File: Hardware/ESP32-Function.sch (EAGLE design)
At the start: 36 parts, among them J1 MICROMOD_STANDARD, Q2 MBT3904DW1T1, U1 EEPROM, U2 ESP-WROOM-3232D-NARROW, U3 3.3V, U4 CP210X

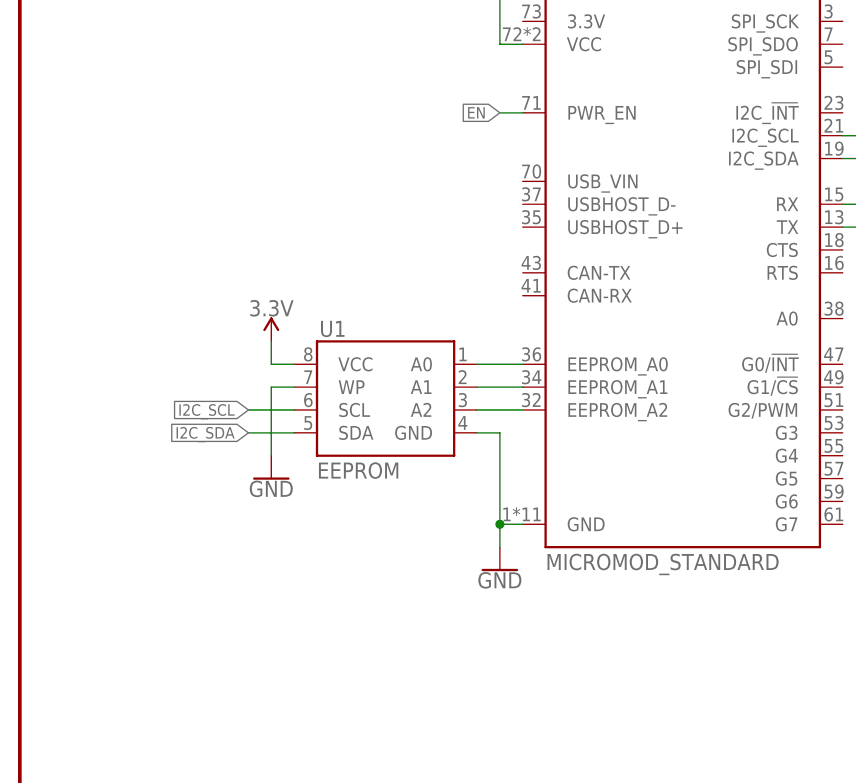
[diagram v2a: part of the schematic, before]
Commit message: Adds pullup resistor and jumper to write protect net, brings write protect trace to card's edge
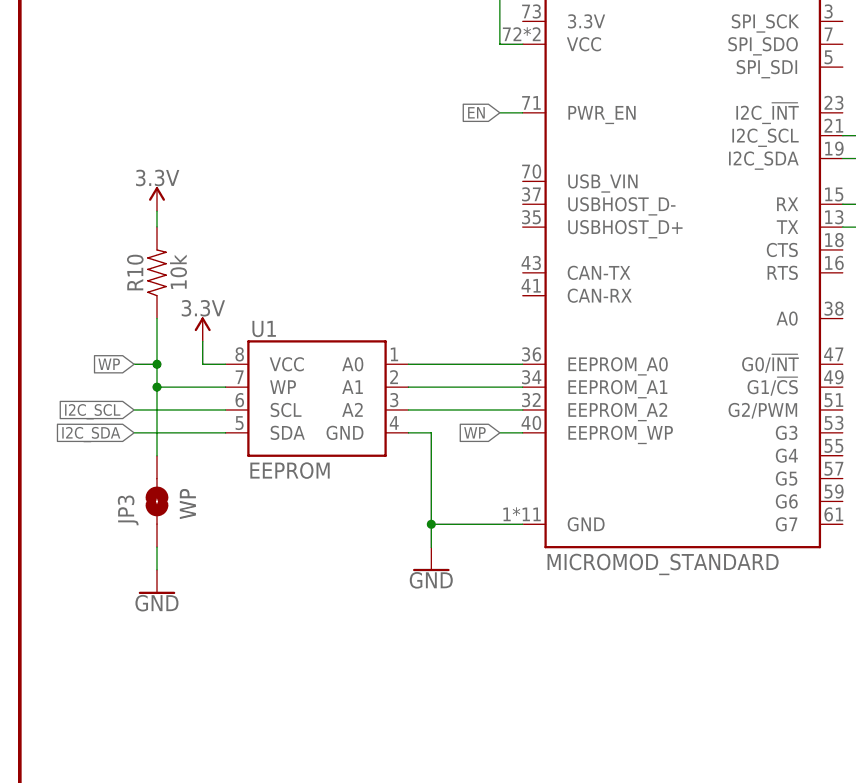
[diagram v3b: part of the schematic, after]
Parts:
- added JP3: JUMPER-SMT_2_NO_SILK, SparkFun-Jumpers:JUMPER-SMT_2_NO_SILK
- added R10: 10k, SparkFun-Resistors:10KOHM-0603-1/10W-1%
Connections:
- new net WP: J1.EEPROM_WP, JP3.2, R10.1, U1.WP
- net 3.3V: now also R10.2
- net GND: now also JP3.1; no longer U1.WP
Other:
- note added: "WP"
- moved on the sheet: U1
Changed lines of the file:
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@@
 <part name="R8" library="SparkFun-Resistors" deviceset="4.7KOHM" device="-0603-1/10W-1%" value="4.7k"/>
 <part name="R9" library="SparkFun-Resistors" deviceset="4.7KOHM" device="-0603-1/10W-1%" value="4.7k"/>
+<part name="R10" library="SparkFun-Resistors" deviceset="10KOHM" device="-0603-1/10W-1%" value="10k"/>
+<part name="JP3" library="SparkFun-Jumpers" deviceset="JUMPER-SMT_2_NO" device="_SILK" package3d_urn="urn:adsk.eagle:package:39279/1"/>
+<part name="SUPPLY10" library="SparkFun-PowerSymbols" deviceset="3.3V" device=""/>
 </parts>
 <sheets>
@@
 remove I2C data line and/or
 clock from pullup resistors.</text>
+<text x="19.558" y="64.008" size="1.778" layer="97" font="vector" rot="R90">WP</text>
 </plain>
 <instances>
@@
 <attribute name="VALUE" x="58.42" y="58.42" size="1.778" layer="96" font="vector"/>
 </instance>
-<instance part="GND1" gate="1" x="53.34" y="58.42" smashed="yes">
-<attribute name="VALUE" x="53.34" y="58.166" size="1.778" layer="96" font="vector" align="top-center"/>
+<instance part="GND1" gate="1" x="45.72" y="58.42" smashed="yes">
+<attribute name="VALUE" x="45.72" y="58.166" size="1.778" layer="96" font="vector" align="top-center"/>
 </instance>
 <instance part="R2" gate="G$1" x="185.42" y="124.46" smashed="yes" rot="R90">
@@
 <attribute name="VALUE" x="274.32" y="59.182" size="1.778" layer="96" font="vector" align="bottom-center"/>
 </instance>
-<instance part="U1" gate="G$1" x="40.64" y="76.2" smashed="yes" rot="MR0">
-<attribute name="NAME" x="33.274" y="84.328" size="1.778" layer="95" font="vector"/>
-<attribute name="VALUE" x="33.02" y="68.58" size="1.778" layer="96" font="vector"/>
-</instance>
-<instance part="SUPPLY3" gate="G$1" x="27.94" y="83.82" smashed="yes">
-<attribute name="VALUE" x="27.94" y="86.614" size="1.778" layer="96" font="vector" align="bottom-center"/>
-</instance>
-<instance part="GND15" gate="1" x="27.94" y="68.58" smashed="yes">
-<attribute name="VALUE" x="27.94" y="68.326" size="1.778" layer="96" font="vector" align="top-center"/>
+<instance part="U1" gate="G$1" x="33.02" y="76.2" smashed="yes" rot="MR0">
+<attribute name="NAME" x="25.654" y="84.328" size="1.778" layer="95" font="vector"/>
+<attribute name="VALUE" x="25.4" y="68.58" size="1.778" layer="96" font="vector"/>
+</instance>
+<instance part="SUPPLY3" gate="G$1" x="20.32" y="83.82" smashed="yes">
+<attribute name="VALUE" x="20.32" y="86.614" size="1.778" layer="96" font="vector" align="bottom-center"/>
+</instance>
+<instance part="GND15" gate="1" x="15.24" y="55.88" smashed="yes">
+<attribute name="VALUE" x="15.24" y="55.626" size="1.778" layer="96" font="vector" align="top-center"/>
 </instance>
 <instance part="U2" gate="U1" x="213.36" y="83.82" smashed="yes">
@@
 <attribute name="NAME" x="366.776" y="195.58" size="1.778" layer="95" font="vector" rot="R90" align="bottom-center"/>
 <attribute name="VALUE" x="369.824" y="195.58" size="1.778" layer="96" font="vector" rot="R90" align="top-center"/>
+</instance>
+<instance part="R10" gate="G$1" x="15.24" y="91.44" smashed="yes" rot="R90">
+<attribute name="NAME" x="13.716" y="91.44" size="1.778" layer="95" font="vector" rot="R90" align="bottom-center"/>
+<attribute name="VALUE" x="16.764" y="91.44" size="1.778" layer="96" font="vector" rot="R90" align="top-center"/>
+</instance>
+<instance part="JP3" gate="G$1" x="15.24" y="66.04" smashed="yes" rot="R90">
+<attribute name="NAME" x="12.7" y="63.5" size="1.778" layer="95" font="vector" rot="R90"/>
+</instance>
+<instance part="SUPPLY10" gate="G$1" x="15.24" y="98.298" smashed="yes">
+<attribute name="VALUE" x="15.24" y="101.092" size="1.778" layer="96" font="vector" align="bottom-center"/>
 </instance>
 </instances>
@@
 <segment>
 <pinref part="U1" gate="G$1" pin="VCC"/>
-<wire x1="30.48" y1="81.28" x2="27.94" y2="81.28" width="0.1524" layer="91"/>
+<wire x1="22.86" y1="81.28" x2="20.32" y2="81.28" width="0.1524" layer="91"/>
 <pinref part="SUPPLY3" gate="G$1" pin="3.3V"/>
-<wire x1="27.94" y1="81.28" x2="27.94" y2="83.82" width="0.1524" layer="91"/>
+<wire x1="20.32" y1="81.28" x2="20.32" y2="83.82" width="0.1524" layer="91"/>
 </segment>
 <segment>
@@
 <pinref part="SUPPLY8" gate="G$1" pin="3.3V"/>
 <wire x1="360.68" y1="210.566" x2="360.68" y2="208.28" width="0.1524" layer="91"/>
+</segment>
+<segment>
+<pinref part="R10" gate="G$1" pin="2"/>
+<pinref part="SUPPLY10" gate="G$1" pin="3.3V"/>
+<wire x1="15.24" y1="98.298" x2="15.24" y2="96.52" width="0.1524" layer="91"/>
 </segment>
 </net>
@@
 </segment>
 <segment>
-<wire x1="53.34" y1="63.5" x2="53.34" y2="60.96" width="0.1524" layer="91"/>
+<wire x1="45.72" y1="63.5" x2="45.72" y2="60.96" width="0.1524" layer="91"/>
 <pinref part="GND1" gate="1" pin="GND"/>
 <pinref part="J1" gate="J1" pin="GND"/>
-<wire x1="55.88" y1="63.5" x2="53.34" y2="63.5" width="0.1524" layer="91"/>
+<wire x1="55.88" y1="63.5" x2="45.72" y2="63.5" width="0.1524" layer="91"/>
 <pinref part="U1" gate="G$1" pin="GND"/>
-<wire x1="50.8" y1="73.66" x2="53.34" y2="73.66" width="0.1524" layer="91"/>
-<wire x1="53.34" y1="73.66" x2="53.34" y2="63.5" width="0.1524" layer="91"/>
-<junction x="53.34" y="63.5"/>
+<wire x1="43.18" y1="73.66" x2="45.72" y2="73.66" width="0.1524" layer="91"/>
+<wire x1="45.72" y1="73.66" x2="45.72" y2="63.5" width="0.1524" layer="91"/>
+<junction x="45.72" y="63.5"/>
 </segment>
 <segment>
@@
 </segment>
 <segment>
-<pinref part="U1" gate="G$1" pin="WP"/>
-<wire x1="30.48" y1="78.74" x2="27.94" y2="78.74" width="0.1524" layer="91"/>
-<wire x1="27.94" y1="78.74" x2="27.94" y2="71.12" width="0.1524" layer="91"/>
+<pinref part="JP3" gate="G$1" pin="1"/>
 <pinref part="GND15" gate="1" pin="GND"/>
+<wire x1="15.24" y1="58.42" x2="15.24" y2="60.96" width="0.1524" layer="91"/>
 </segment>
 </net>
@@
 <segment>
 <pinref part="U1" gate="G$1" pin="SCL"/>
-<wire x1="30.48" y1="76.2" x2="25.4" y2="76.2" width="0.1524" layer="91"/>
-<label x="25.4" y="76.2" size="1.27" layer="95" font="vector" rot="R180" xref="yes"/>
+<wire x1="22.86" y1="76.2" x2="12.7" y2="76.2" width="0.1524" layer="91"/>
+<label x="12.7" y="76.2" size="1.27" layer="95" font="vector" rot="R180" xref="yes"/>
 </segment>
 <segment>
@@
 <segment>
 <pinref part="U1" gate="G$1" pin="SDA"/>
-<wire x1="30.48" y1="73.66" x2="25.4" y2="73.66" width="0.1524" layer="91"/>
-<label x="25.4" y="73.66" size="1.27" layer="95" font="vector" rot="R180" xref="yes"/>
+<wire x1="22.86" y1="73.66" x2="12.7" y2="73.66" width="0.1524" layer="91"/>
+<label x="12.7" y="73.66" size="1.27" layer="95" font="vector" rot="R180" xref="yes"/>
 </segment>
 <segment>
@@
 <pinref part="J1" gate="J1" pin="EEPROM_A2"/>
 <pinref part="U1" gate="G$1" pin="A2"/>
-<wire x1="55.88" y1="76.2" x2="50.8" y2="76.2" width="0.1524" layer="91"/>
+<wire x1="55.88" y1="76.2" x2="43.18" y2="76.2" width="0.1524" layer="91"/>
 </segment>
 </net>
@@
 <pinref part="J1" gate="J1" pin="EEPROM_A1"/>
 <pinref part="U1" gate="G$1" pin="A1"/>
-<wire x1="55.88" y1="78.74" x2="50.8" y2="78.74" width="0.1524" layer="91"/>
+<wire x1="55.88" y1="78.74" x2="43.18" y2="78.74" width="0.1524" layer="91"/>
 </segment>
 </net>
@@
 <pinref part="J1" gate="J1" pin="EEPROM_A0"/>
 <pinref part="U1" gate="G$1" pin="A0"/>
-<wire x1="55.88" y1="81.28" x2="50.8" y2="81.28" width="0.1524" layer="91"/>
+<wire x1="55.88" y1="81.28" x2="43.18" y2="81.28" width="0.1524" layer="91"/>
 </segment>
 </net>
@@
 </segment>
 </net>
+<net name="WP" class="0">
+<segment>
+<pinref part="J1" gate="J1" pin="EEPROM_WP"/>
+<wire x1="53.34" y1="73.66" x2="55.88" y2="73.66" width="0.1524" layer="91"/>
+<label x="53.34" y="73.66" size="1.27" layer="95" rot="R180" xref="yes"/>
+</segment>
+<segment>
+<pinref part="U1" gate="G$1" pin="WP"/>
+<wire x1="22.86" y1="78.74" x2="15.24" y2="78.74" width="0.1524" layer="91"/>
+<pinref part="R10" gate="G$1" pin="1"/>
+<wire x1="15.24" y1="78.74" x2="15.24" y2="81.28" width="0.1524" layer="91"/>
+<wire x1="15.24" y1="81.28" x2="15.24" y2="86.36" width="0.1524" layer="91"/>
+<wire x1="15.24" y1="78.74" x2="15.24" y2="71.12" width="0.1524" layer="91"/>
+<junction x="15.24" y="78.74"/>
+<pinref part="JP3" gate="G$1" pin="2"/>
+<wire x1="12.7" y1="81.28" x2="15.24" y2="81.28" width="0.1524" layer="91"/>
+<junction x="15.24" y="81.28"/>
+<label x="12.7" y="81.28" size="1.27" layer="95" rot="R180" xref="yes"/>
+</segment>
+</net>
